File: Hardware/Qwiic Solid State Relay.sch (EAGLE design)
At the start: 49 parts, among them J2 Qwiic Right Angle, J3 Qwiic Right Angle, J9 AVR_SPI_PROG_3X2TESTPOINTS, K1 Solid State Relay - 40A, K2 Solid State Relay - 40A, K3 Solid State Relay - 40A, K4 Solid State Relay - 40A, Q1 600mA/40V, Q2 600mA/40V, Q3 600mA/40V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

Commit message: adding silk
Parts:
- LOGO1: value SFE_LOGO_NAME_FLAME.1_INCH -> SFE_LOGO_NAME1_INCH; device SparkFun-Aesthetics:SFE_LOGO_NAME_FLAME.1_INCH -> SparkFun-Aesthetics:SFE_LOGO_NAME1_INCH
- R12, R2, R5, R8: value 33 -> 47; device SparkFun-Resistors:33OHM-0603-1/10W-1% -> SparkFun-Resistors:47OHM-0603-1/10W-1%
- renumbered JP1 to I2C, JP2 to PWR, JP3 to ADR
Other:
- note added: "Andy England"
- note added: "Cut jumper to remove I2C pullups from bus"
- note added: "v10"
- note removed: "Elias Santistevan"
- note removed: "v20"

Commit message: updating for reds after design review, checklist
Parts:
- added J4: (no value), SparkFun-Connectors:CONN_01PTH_NO_SILK_YES_STOP
- added JP1, JP2, JP3, JP8: STAND-OFF, SparkFun-Hardware:STAND-OFF
- ADR, PWR: value JUMPER-SMT_2_NO_SILK -> JUMPER-SMT_2_NC_TRACE_SILK; device SparkFun-Jumpers:JUMPER-SMT_2_NO_SILK -> SparkFun-Jumpers:JUMPER-SMT_2_NC_TRACE_SILK
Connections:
- net !RESET: now also J4.1
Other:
- note added: "VIN: 2.7-5.5V"
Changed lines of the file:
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@@
 <part name="LOGO2" library="SparkFun-Aesthetics" deviceset="OSHW-LOGO" device="S" value="OSHW-LOGOS"/>
 <part name="GND18" library="SparkFun-PowerSymbols" deviceset="GND" device=""/>
-<part name="ADR" library="SparkFun-Jumpers" deviceset="JUMPER-SMT_2_NO" device="_SILK" package3d_urn="urn:adsk.eagle:package:39279/1"/>
-<part name="PWR" library="SparkFun-Jumpers" deviceset="JUMPER-SMT_2_NO" device="_SILK" package3d_urn="urn:adsk.eagle:package:39279/1"/>
+<part name="ADR" library="SparkFun-Jumpers" deviceset="JUMPER-SMT_2_NC_TRACE" device="_SILK" package3d_urn="urn:adsk.eagle:package:39281/1"/>
+<part name="PWR" library="SparkFun-Jumpers" deviceset="JUMPER-SMT_2_NC_TRACE" device="_SILK" package3d_urn="urn:adsk.eagle:package:39281/1"/>
 <part name="GND7" library="SparkFun-PowerSymbols" deviceset="GND" device=""/>
 <part name="GND1" library="SparkFun-PowerSymbols" deviceset="GND" device=""/>
@@
 <part name="SUPPLY13" library="SparkFun-PowerSymbols" deviceset="3.3V" device=""/>
 <part name="LOGO1" library="SparkFun-Aesthetics" deviceset="SFE_LOGO_NAME" device="1_INCH"/>
+<part name="J4" library="SparkFun-Connectors" deviceset="CONN_01" device="PTH_NO_SILK_YES_STOP"/>
+<part name="JP1" library="SparkFun-Hardware" deviceset="STAND-OFF" device=""/>
+<part name="JP2" library="SparkFun-Hardware" deviceset="STAND-OFF" device=""/>
+<part name="JP3" library="SparkFun-Hardware" deviceset="STAND-OFF" device=""/>
+<part name="JP8" library="SparkFun-Hardware" deviceset="STAND-OFF" device=""/>
 </parts>
 <sheets>
@@
 <text x="236.728" y="8.636" size="2.54" layer="94" font="vector">v10</text>
 <text x="2.54" y="114.3" size="2.54" layer="94" font="vector">Connectors</text>
-<text x="157.48" y="114.3" size="2.54" layer="94" font="vector">ATtiny84</text>
+<text x="149.86" y="114.3" size="2.54" layer="94" font="vector">ATtiny84</text>
 <text x="63.5" y="114.3" size="2.54" layer="94" font="vector">Programming Header</text>
 <text x="101.6" y="2.54" size="1.27" layer="97" font="vector">Address 0x6D: HIGH (Default)
@@
 <text x="105.664" y="62.738" size="1.27" layer="97" font="vector">Cut jumper to remove
 I2C pullups from bus</text>
+<text x="149.86" y="111.76" size="1.778" layer="94" font="vector">VIN: 2.7-5.5V</text>
 </plain>
 <instances>
@@
 </instance>
 <instance part="LOGO1" gate="G$1" x="157.48" y="40.64" smashed="yes"/>
+<instance part="J4" gate="G$1" x="38.1" y="20.32" smashed="yes" rot="R180">
+<attribute name="VALUE" x="40.64" y="25.146" size="1.778" layer="96" font="vector" rot="R180"/>
+<attribute name="NAME" x="40.64" y="17.272" size="1.778" layer="95" font="vector" rot="R180"/>
+</instance>
+<instance part="JP1" gate="G$1" x="244.348" y="31.496" smashed="yes"/>
+<instance part="JP2" gate="G$1" x="244.348" y="28.956" smashed="yes"/>
+<instance part="JP3" gate="G$1" x="246.888" y="28.956" smashed="yes"/>
+<instance part="JP8" gate="G$1" x="246.888" y="31.496" smashed="yes"/>
 </instances>
 <busses>
@@
 <junction x="218.44" y="99.06"/>
 </segment>
+<segment>
+<pinref part="J4" gate="G$1" pin="1"/>
+<wire x1="30.48" y1="20.32" x2="27.94" y2="20.32" width="0.1524" layer="91"/>
+<label x="27.94" y="20.32" size="1.27" layer="95" font="vector" rot="R180" xref="yes"/>
+</segment>
 </net>

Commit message: adding panel
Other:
- note added: "Address 0x6D: HIGH (Close Jumper) Address 0x6C: LOW (Default)"
- note removed: "Address 0x6D: HIGH (Default) Address 0x6C: LOW (Close Jumper)"
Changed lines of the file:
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@@
 <text x="149.86" y="114.3" size="2.54" layer="94" font="vector">ATtiny84</text>
 <text x="63.5" y="114.3" size="2.54" layer="94" font="vector">Programming Header</text>
-<text x="101.6" y="2.54" size="1.27" layer="97" font="vector">Address 0x6D: HIGH (Default)
-Address 0x6C: LOW (Close Jumper)</text>
+<text x="101.6" y="2.54" size="1.27" layer="97" font="vector">Address 0x6D: HIGH (Close Jumper)
+Address 0x6C: LOW (Default)</text>
 <wire x1="119.38" y1="12.7" x2="119.38" y2="7.62" width="0.2032" layer="97" style="dashdot"/>
 <text x="115.824" y="24.638" size="1.27" layer="97" font="vector">Cut jumper

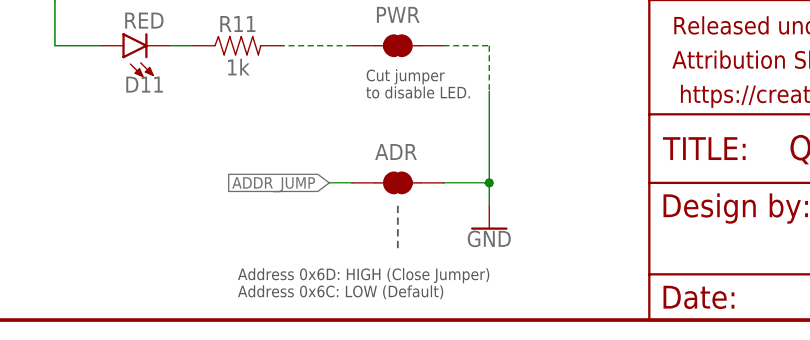
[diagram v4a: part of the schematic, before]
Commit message: updating schematic address note
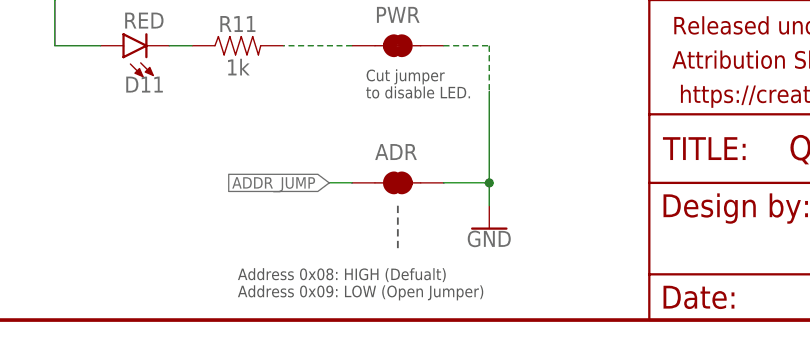
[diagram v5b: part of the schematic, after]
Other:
- note added: "Address 0x08: HIGH (Defualt) Address 0x09: LOW (Open Jumper)"
- note removed: "Address 0x6D: HIGH (Close Jumper) Address 0x6C: LOW (Default)"
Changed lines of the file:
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@@
 <text x="149.86" y="114.3" size="2.54" layer="94" font="vector">ATtiny84</text>
 <text x="63.5" y="114.3" size="2.54" layer="94" font="vector">Programming Header</text>
-<text x="101.6" y="2.54" size="1.27" layer="97" font="vector">Address 0x6D: HIGH (Close Jumper)
-Address 0x6C: LOW (Default)</text>
+<text x="101.6" y="2.54" size="1.27" layer="97" font="vector">Address 0x08: HIGH (Defualt)
+Address 0x09: LOW (Open Jumper)</text>
 <wire x1="119.38" y1="12.7" x2="119.38" y2="7.62" width="0.2032" layer="97" style="dashdot"/>
 <text x="115.824" y="24.638" size="1.27" layer="97" font="vector">Cut jumper
